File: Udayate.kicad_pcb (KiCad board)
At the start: 4 copper layers, 60.1 x 60 mm, 114 parts, among them J501 12402012E212A, J502 Conn_01x03_Pin, J503 Conn_01x03_Pin, J504 Conn_01x03_Pin, J505 Conn_01x03_Pin, J506 Conn_01x03_Pin, J507 Conn_01x03_Pin, J508 Conn_01x03_Pin, J509 Conn_01x03_Pin, J601 Conn_01x04_Socket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

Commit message: fix: repositioned R24 - R206 & add silk screen for 5V input
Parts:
- removed REF**: OSHW-Logo2_14.6x12mm_SilkScreen, Symbol:OSHW-Logo2_14.6x12mm_SilkScreen
- moved R205 6.22 mm to (134.9, 106.2), turned to 45 degrees
- moved R206 4.88 mm to (136.1, 107.4), turned to 45 degrees
- moved R204 3.56 mm to (137.3, 108.6), turned to 45 degrees
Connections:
- R204 pad 1: /IO/D_MOUT_1 -> /IO/D_MOUT_3
- R205 pad 1: /IO/D_MOUT_2 -> /IO/D_MOUT_1
- R206 pad 1: /IO/D_MOUT_3 -> /IO/D_MOUT_2
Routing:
- net /MCU/D_TIM2_CH2: track 13.3 -> 6.63 mm
- net /IO/D_MOUT_2: track 7.35 -> 13.1 mm
- net /MCU/D_TIM2_CH3: track 11.4 -> 6.06 mm
- net /IO/D_MOUT_3: track 11.2 -> 15.7 mm
- net /MCU/D_TIM2_CH1: track 14.1 -> 10.3 mm
- net /IO/D_MOUT_1: track 11.2 -> 10.6 mm
- net GND: vias 183 -> 186

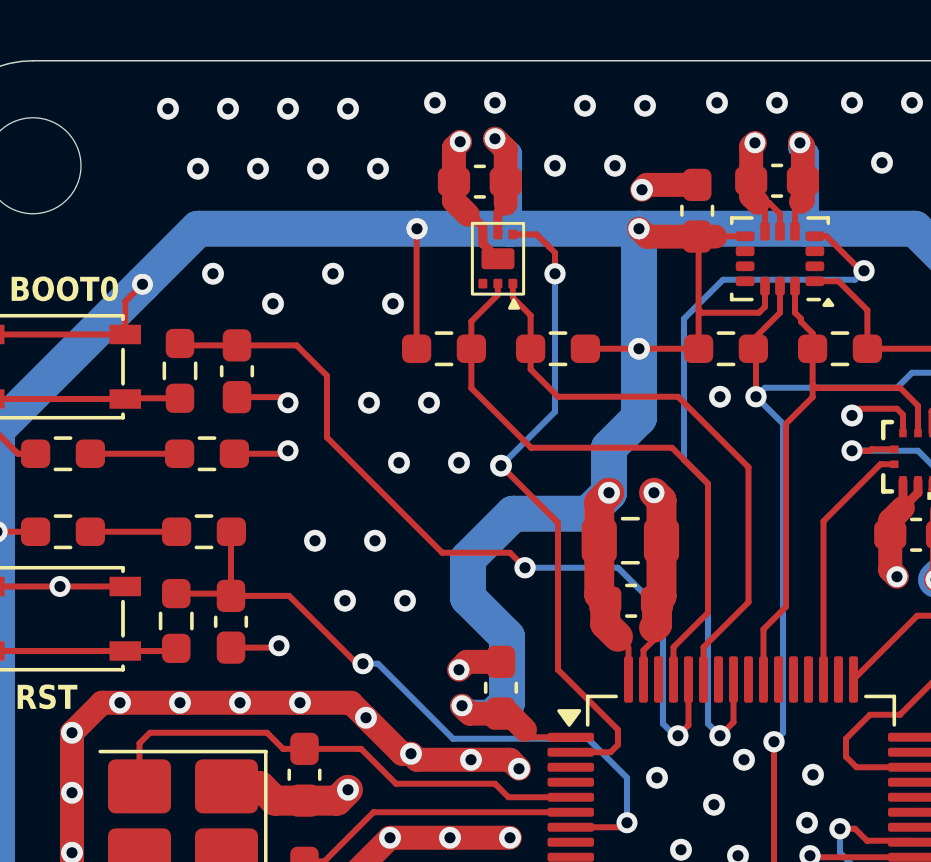
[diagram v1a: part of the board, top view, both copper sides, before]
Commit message: fix: fix magnetometer pinout
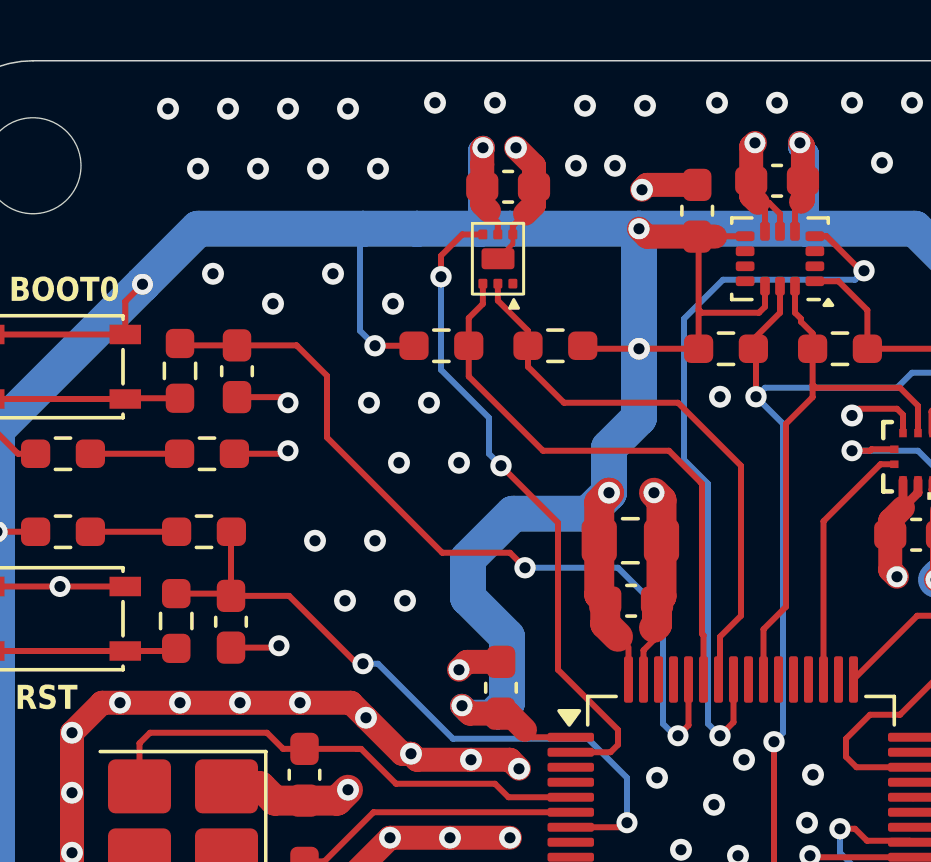
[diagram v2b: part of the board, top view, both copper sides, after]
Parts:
- moved R222 3.89 mm to (135.7, 81.5), turned to 0 degrees
- moved R221 3.71 mm to (139.5, 81.5), turned to 180 degrees
- moved C305 0.96 mm to (137.9, 76.2), turned to 0 degrees
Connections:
- U201 pad 58: unconnected-(U201-PB6-Pad58) -> /IMUs/D_I2C1_SCL
- U201 pad 61: /IMUs/D_I2C1_SCL -> unconnected-(U201-PB8-Pad61)
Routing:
- net /IMUs/D_I2C1_SCL: track 20.1 -> 19.1 mm
- net +3V3: track 319.2 -> 320.1 mm

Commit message: fix: update rev version silkscreen on PCB
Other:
- board text added: "Rev: 1.1"
- board text removed: "Rev: 1"
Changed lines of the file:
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@@
 		)
 	)
-	(gr_text "Rev: 1"
+	(gr_text "Rev: 1.1"
 		(at 151.55 106.65 0)
 		(layer "B.SilkS" knockout)
